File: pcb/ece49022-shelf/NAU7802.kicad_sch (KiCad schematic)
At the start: 18 parts, among them IC1 NAU7802

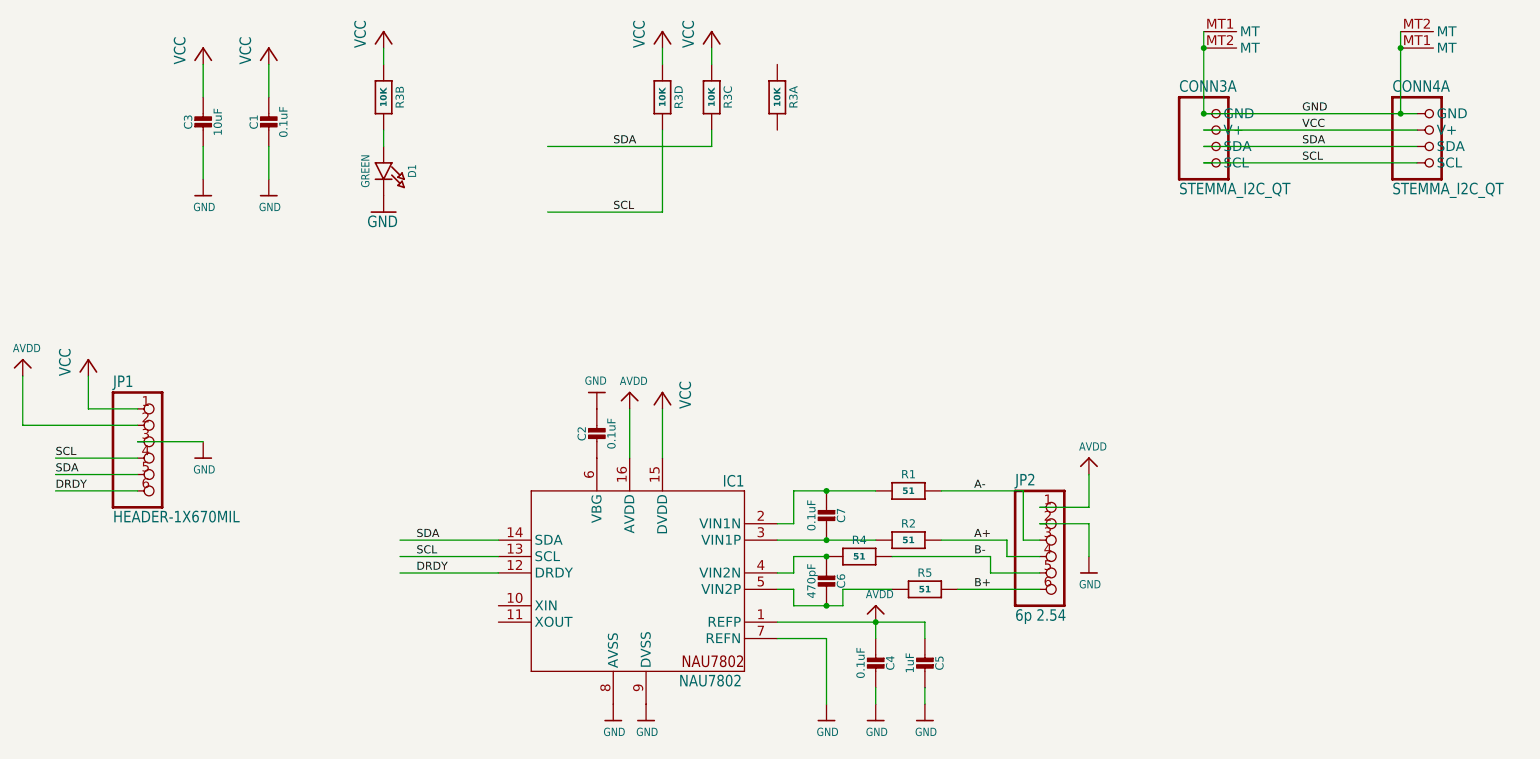
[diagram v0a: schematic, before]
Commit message: Removed Breakout Board
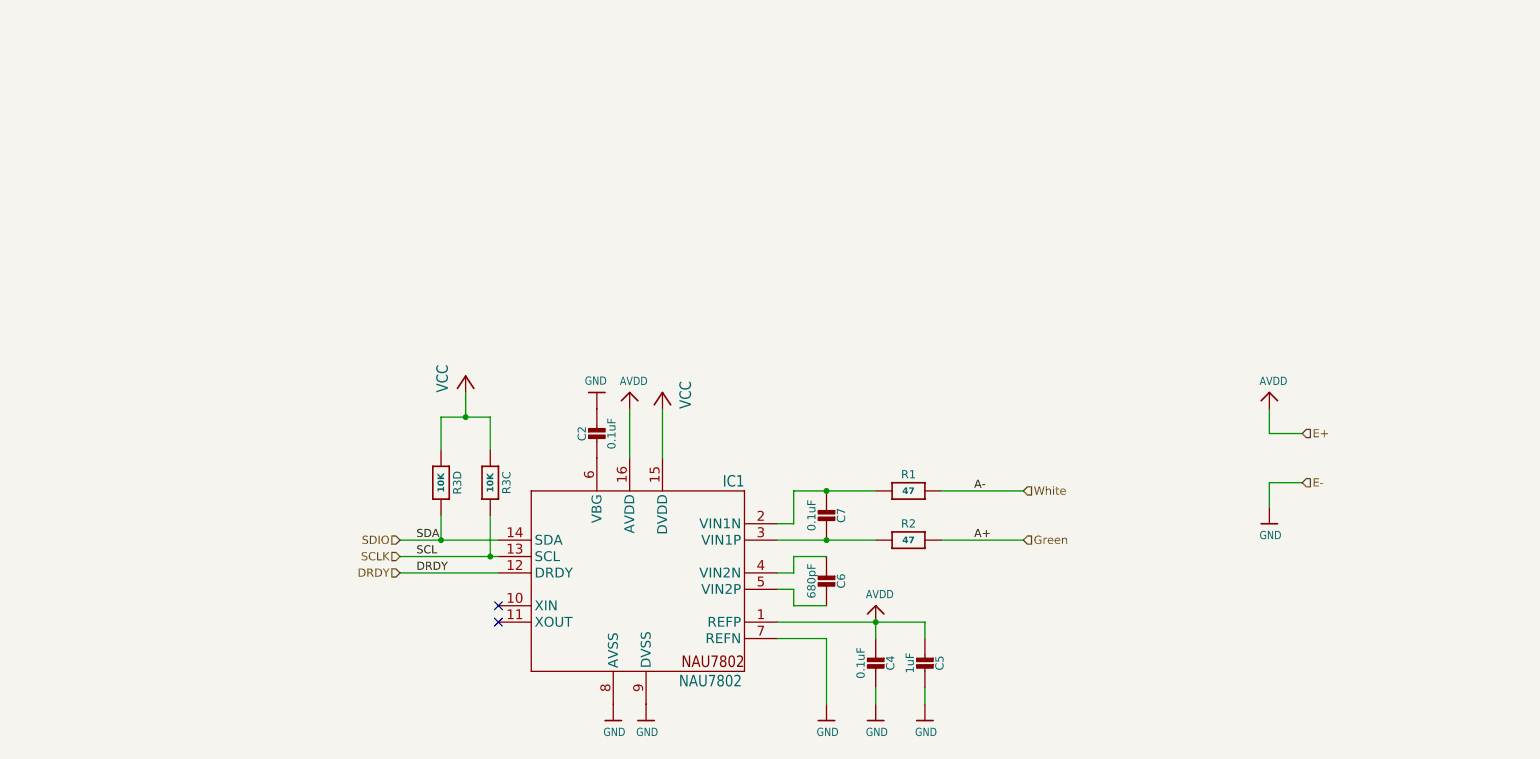
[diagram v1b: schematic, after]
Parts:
- removed C1: 0.1uF, NAU7802:0603-NO, symbol NAU7802-eagle-import:CAP_CERAMIC0603_NO
- removed C3: 10uF, NAU7802:0805-NO, symbol NAU7802-eagle-import:CAP_CERAMIC0805-NOOUTLINE
- removed CONN3, CONN4: STEMMA_I2C_QT, NAU7802:JST_SH4, symbol NAU7802-eagle-import:STEMMA_I2C_QT
- removed D1: GREEN, NAU7802:CHIPLED_0603_NOOUTLINE, symbol NAU7802-eagle-import:LED0603_NOOUTLINE
- removed JP1: HEADER-1X670MIL, NAU7802:1X06_ROUND_70, symbol NAU7802-eagle-import:HEADER-1X670MIL
- removed JP2: 6p 2.54, NAU7802:1X06_2.54MMTERMINAL, symbol NAU7802-eagle-import:HEADER-1X6_2.54MMTERM
- removed unit 1 of R3
- removed unit 2 of R3
- removed R4, R5: 51, NAU7802:0603-NO, symbol NAU7802-eagle-import:RESISTOR_0603_NOOUT
- C6: value 470pF -> 680pF
- R1, R2: value 51 -> 47
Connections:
- net A+ renamed Green
- net A- renamed White
- net SCL renamed SCLK
- net SCLK: now also R3.6 (2); no longer R3.5 (2)
- net SDA renamed SDIO
- net SDIO: now also R3.5 (2); no longer R3.6 (2)
- no-connect marks 0 -> 2
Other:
- moved on the sheet: R3C, R3D

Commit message: Schematic
update
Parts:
- removed C2, C4, C7: 0.1uF, NAU7802:0603-NO, symbol NAU7802-eagle-import:CAP_CERAMIC0603_NO
- removed C5: 1uF, NAU7802:0603-NO, symbol NAU7802-eagle-import:CAP_CERAMIC0603_NO
- removed C6: 680pF, NAU7802:0603-NO, symbol NAU7802-eagle-import:CAP_CERAMIC0603_NO
- removed R1, R2: 47, NAU7802:0603-NO, symbol NAU7802-eagle-import:RESISTOR_0603_NOOUT
- removed R3: 10K, NAU7802:RESPACK_4X0603, symbol NAU7802-eagle-import:RESISTOR_4PACK
- added C1: 680pF, 50V, symbol Device:C_Small
- added C2, C3, C5: 0.1uF, 16V, symbol Device:C_Small
- added C4: 1uF, 10V, symbol Device:C_Small
- added R1, R2: 47, 0.1%, Resistor_SMD:R_0402_1005Metric_Pad0.72x0.64mm_HandSolder, symbol Device:R_US
- added R3, R4: 10K, 1%, Resistor_SMD:R_0402_1005Metric_Pad0.72x0.64mm_HandSolder, symbol Device:R_US
- IC1: footprint NAU7802:SOIC16_NARROW -> 49022_Footprints:SOI16_NAU7802SGI_NUV-M
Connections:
- net AVDD: now also C3.1, C4.1
- net GND: now also C3.2, C4.2, C5.1
- net Green: now also R2.2
- net SCLK: now also R4.1
- net SDIO: now also R3.1
- net VCC: now also R3.2, R4.2
- net White: now also R1.2
- net at IC1.3 (VIN1P): now also C2.2, R2.1
- net at IC1.2 (VIN1N): now also C2.1, R1.1
- net at IC1.4 (VIN2N): now also C1.1
- net at IC1.5 (VIN2P): now also C1.2
- net at IC1.6 (VBG): now also C5.2

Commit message: Update NAU7802.kicad_sch
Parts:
- C2, C3, C5: value 0.1uF, 16V -> 0.1uF, 25V
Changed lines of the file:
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@@
 	(symbol
 		(lib_id "Device:C_Small")
-		(at 172.72 125.73 0)
-		(unit 1)
-		(exclude_from_sim no)
-		(in_bom yes)
-		(on_board yes)
-		(dnp no)
-		(property "Reference" "C3"
-			(at 175.514 126.746 90)
+		(at 129.54 90.17 0)
+		(unit 1)
+		(exclude_from_sim no)
+		(in_bom yes)
+		(on_board yes)
+		(dnp no)
+		(property "Reference" "C5"
+			(at 132.334 91.186 90)
 			(effects
 				(font
@@
 			)
 		)
-		(property "Value" "0.1uF, 16V"
-			(at 169.672 131.064 90)
+		(property "Value" "0.1uF, 25V"
+			(at 126.492 95.504 90)
 			(effects
 				(font
@@
 		)
 		(property "Footprint" ""
-			(at 172.72 125.73 0)
+			(at 129.54 90.17 0)
 			(effects
 				(font
@@
 		)
 		(property "Datasheet" "~"
-			(at 172.72 125.73 0)
-			(effects
-				(font
-					(size 1.27 1.27)
-				)
-				(hide yes)
-			)
-		)
-		(property "Description" "Unpolarized capacitor, small symbol"
-			(at 172.72 125.73 0)
+			(at 129.54 90.17 0)
+			(effects
+				(font
+					(size 1.27 1.27)
+				)
+				(hide yes)
+			)
+		)
+		(property "Description" "0402B104K250HI"
+			(at 129.54 90.17 0)
 			(effects
 				(font
@@
 			(project "ece49022-shelf"
 				(path "/cb6cb1b4-c151-4aa2-8cd7-5430288cfa02/fb213d7f-28bb-4d6d-ba03-4017b4d07db5"
-					(reference "C3")
+					(reference "C5")
 					(unit 1)
 				)
@@
 				(path "/cb6cb1b4-c151-4aa2-8cd7-5430288cfa02/fb213d7f-28bb-4d6d-ba03-4017b4d07db5"
 					(reference "R2")
-					(unit 1)
-				)
-			)
-		)
-	)
-	(symbol
-		(lib_id "Device:C_Small")
-		(at 129.54 90.17 0)
-		(unit 1)
-		(exclude_from_sim no)
-		(in_bom yes)
-		(on_board yes)
-		(dnp no)
-		(property "Reference" "C5"
-			(at 132.334 91.186 90)
-			(effects
-				(font
-					(size 1.27 1.27)
-				)
-				(justify left)
-			)
-		)
-		(property "Value" "0.1uF, 16V"
-			(at 126.492 95.504 90)
-			(effects
-				(font
-					(size 1.27 1.27)
-				)
-				(justify left)
-			)
-		)
-		(property "Footprint" ""
-			(at 129.54 90.17 0)
-			(effects
-				(font
-					(size 1.27 1.27)
-				)
-				(hide yes)
-			)
-		)
-		(property "Datasheet" "~"
-			(at 129.54 90.17 0)
-			(effects
-				(font
-					(size 1.27 1.27)
-				)
-				(hide yes)
-			)
-		)
-		(property "Description" "Unpolarized capacitor, small symbol"
-			(at 129.54 90.17 0)
-			(effects
-				(font
-					(size 1.27 1.27)
-				)
-				(hide yes)
-			)
-		)
-		(pin "1"
-		)
-		(pin "2"
-		)
-		(instances
-			(project "ece49022-shelf"
-				(path "/cb6cb1b4-c151-4aa2-8cd7-5430288cfa02/fb213d7f-28bb-4d6d-ba03-4017b4d07db5"
-					(reference "C5")
 					(unit 1)
 				)
@@
 	)
 	(symbol
+		(lib_id "Device:C_Small")
+		(at 172.72 125.73 0)
+		(unit 1)
+		(exclude_from_sim no)
+		(in_bom yes)
+		(on_board yes)
+		(dnp no)
+		(property "Reference" "C3"
+			(at 175.514 126.746 90)
+			(effects
+				(font
+					(size 1.27 1.27)
+				)
+				(justify left)
+			)
+		)
+		(property "Value" "0.1uF, 25V"
+			(at 169.672 131.064 90)
+			(effects
+				(font
+					(size 1.27 1.27)
+				)
+				(justify left)
+			)
+		)
+		(property "Footprint" ""
+			(at 172.72 125.73 0)
+			(effects
+				(font
+					(size 1.27 1.27)
+				)
+				(hide yes)
+			)
+		)
+		(property "Datasheet" "~"
+			(at 172.72 125.73 0)
+			(effects
+				(font
+					(size 1.27 1.27)
+				)
+				(hide yes)
+			)
+		)
+		(property "Description" "0402B104K250HI"
+			(at 172.72 125.73 0)
+			(effects
+				(font
+					(size 1.27 1.27)
+				)
+				(hide yes)
+			)
+		)
+		(pin "1"
+		)
+		(pin "2"
+		)
+		(instances
+			(project "ece49022-shelf"
+				(path "/cb6cb1b4-c151-4aa2-8cd7-5430288cfa02/fb213d7f-28bb-4d6d-ba03-4017b4d07db5"
+					(reference "C3")
+					(unit 1)
+				)
+			)
+		)
+	)
+	(symbol
 		(lib_id "power:GND")
 		(at 217.17 102.87 0)
@@
 			)
 		)
-		(property "Value" "0.1uF, 16V"
+		(property "Value" "0.1uF, 25V"
 			(at 165.862 108.204 90)
 			(effects
@@
 			)
 		)
-		(property "Description" "Unpolarized capacitor, small symbol"
+		(property "Description" "0402B104K250HI"
 			(at 168.91 102.87 0)
 			(effects
@@
 			)
 		)
-		(property "Description" "Unpolarized capacitor, small symbol"
+		(property "Description" "0402W105K100HI"
 			(at 180.34 125.73 0)
 			(effects
